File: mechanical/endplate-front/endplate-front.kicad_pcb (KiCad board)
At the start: 2 copper layers, 88 x 38 mm, 0 parts

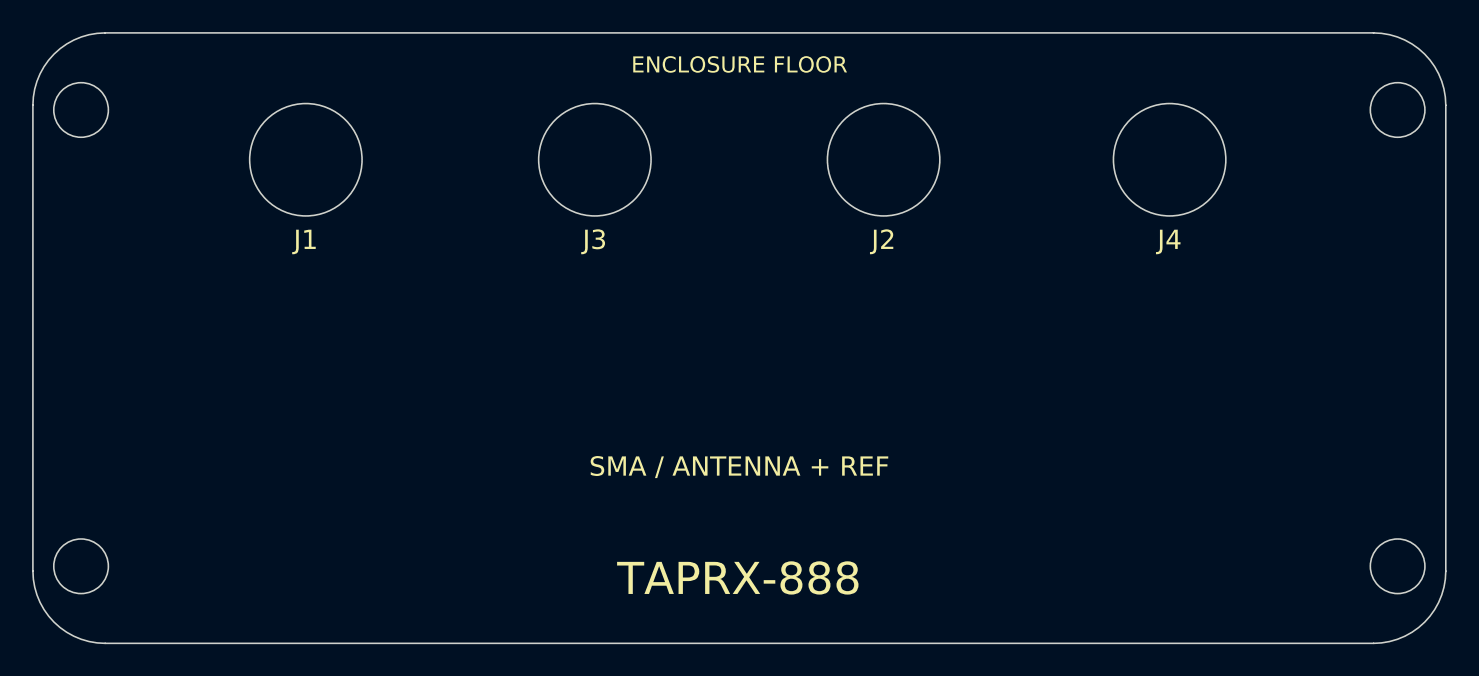
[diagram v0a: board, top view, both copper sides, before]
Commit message: mechanical: label front-plate SMA cutouts by function
Silkscreen the four SMA pass-throughs with their functions instead of bare
designators: J1 RF IN, J3 SPARE, J2 TIMESYNC IN, J4 EXT REF (function name +
small Jx under each hole).

Co-Authored-By: Claude Opus 4.8 <noreply@anthropic.com>
Claude-Session: https://claude.ai/code/session_019A4jkTeNPLki8CdfTWEUwM
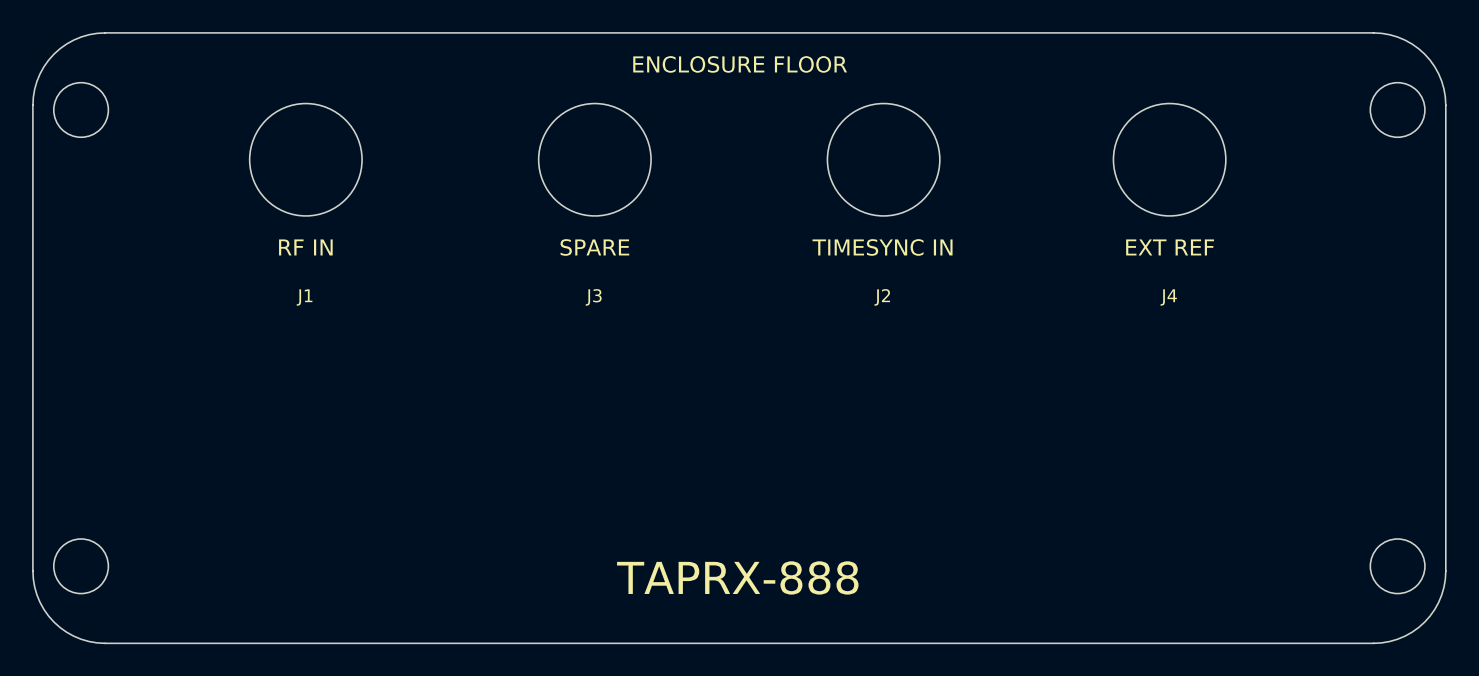
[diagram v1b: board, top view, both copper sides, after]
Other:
- board text added: "EXT REF"
- board text added: "RF IN"
- board text added: "SPARE"
- board text added: "TIMESYNC IN"
- board text removed: "SMA / ANTENNA + REF"
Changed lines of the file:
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@@
 		(layer "Edge.Cuts")
 	)
-	(gr_text "J1"
-		(at 17.0 12.9)
+	(gr_text "RF IN"
+		(at 17.0 13.4)
 		(layer "F.SilkS")
 		(effects
 			(font
-				(size 1.2 1.2)
-				(thickness 0.2)
+				(size 1.0 1.0)
+				(thickness 0.15)
+			)
+		)
+	)
+	(gr_text "J1"
+		(at 17.0 16.4)
+		(layer "F.SilkS")
+		(effects
+			(font
+				(size 0.8 0.8)
+				(thickness 0.12)
 			)
 		)
@@
 		(layer "Edge.Cuts")
 	)
-	(gr_text "J3"
-		(at 35.0 12.9)
+	(gr_text "SPARE"
+		(at 35.0 13.4)
 		(layer "F.SilkS")
 		(effects
 			(font
-				(size 1.2 1.2)
-				(thickness 0.2)
+				(size 1.0 1.0)
+				(thickness 0.15)
+			)
+		)
+	)
+	(gr_text "J3"
+		(at 35.0 16.4)
+		(layer "F.SilkS")
+		(effects
+			(font
+				(size 0.8 0.8)
+				(thickness 0.12)
 			)
 		)
@@
 		(layer "Edge.Cuts")
 	)
-	(gr_text "J2"
-		(at 52.986 12.9)
+	(gr_text "TIMESYNC IN"
+		(at 52.986 13.4)
 		(layer "F.SilkS")
 		(effects
 			(font
-				(size 1.2 1.2)
-				(thickness 0.2)
+				(size 1.0 1.0)
+				(thickness 0.15)
+			)
+		)
+	)
+	(gr_text "J2"
+		(at 52.986 16.4)
+		(layer "F.SilkS")
+		(effects
+			(font
+				(size 0.8 0.8)
+				(thickness 0.12)
 			)
 		)
@@
 		(layer "Edge.Cuts")
 	)
-	(gr_text "J4"
-		(at 70.8 12.9)
+	(gr_text "EXT REF"
+		(at 70.8 13.4)
 		(layer "F.SilkS")
 		(effects
 			(font
-				(size 1.2 1.2)
-				(thickness 0.2)
+				(size 1.0 1.0)
+				(thickness 0.15)
+			)
+		)
+	)
+	(gr_text "J4"
+		(at 70.8 16.4)
+		(layer "F.SilkS")
+		(effects
+			(font
+				(size 0.8 0.8)
+				(thickness 0.12)
 			)
 		)
@@
 			)
 		)
-	)
-	(gr_text "SMA / ANTENNA + REF"
-		(at 44.0 27.02)
-		(layer "F.SilkS")
-		(effects
-			(font
-				(size 1.2 1.2)
-				(thickness 0.2)
-			)
-		)

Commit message: mechanical: move connector labels to the floor side (exposed panel)
The interior side of each cutout is hidden behind the board once assembled, so
put the silkscreen on the floor side (toward the top edge): SMA function names
above their holes, USB label above its opening. Drop the per-hole J# from silk
(space is tight on the exposed strip) and record the J#->function map + floor
orientation in the Cmts.User note instead.

Co-Authored-By: Claude Opus 4.8 <noreply@anthropic.com>
Claude-Session: https://claude.ai/code/session_019A4jkTeNPLki8CdfTWEUwM
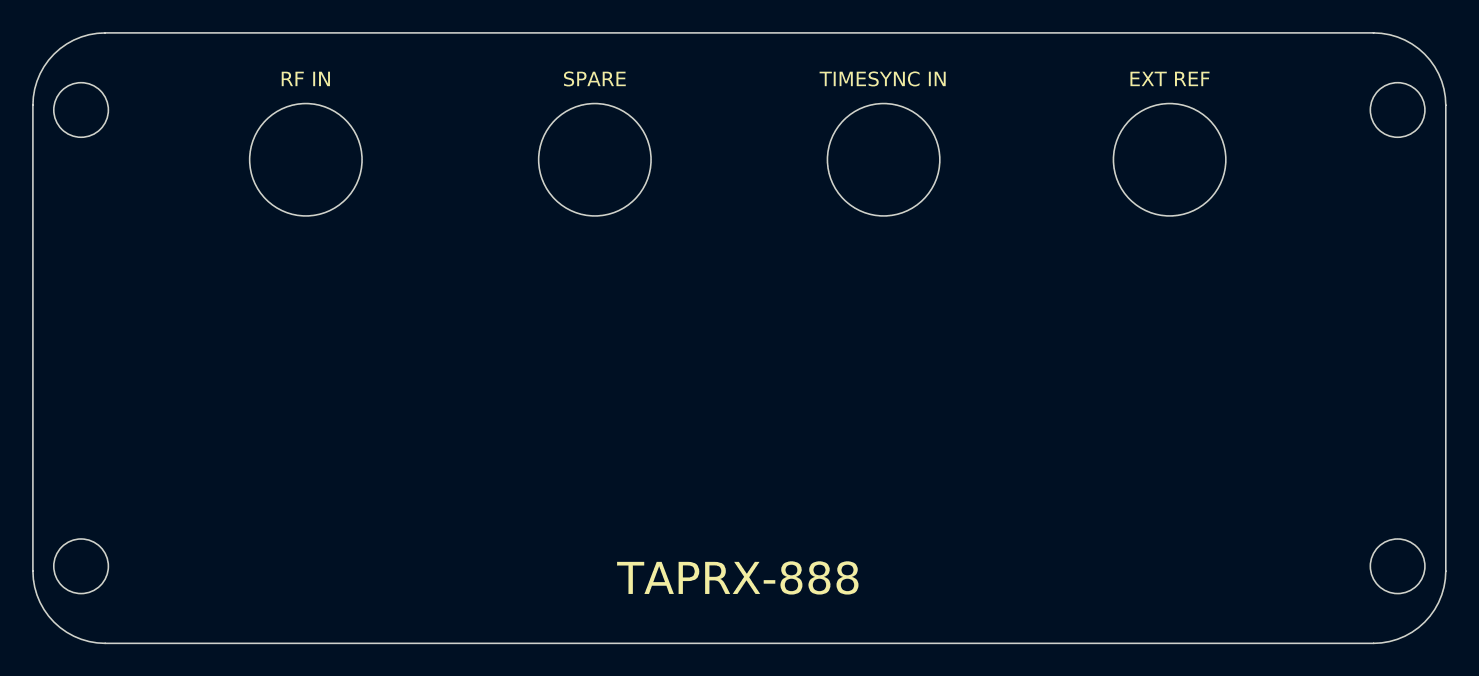
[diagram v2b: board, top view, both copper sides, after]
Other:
- board text added: "Outline+M3 corner holes from enclosure DXF (88x38 R4.5, holes Ø3.4 @ +/-41,+/-14.21). Connector Y set from measured 7.9mm PCB rail height above enclosure floor (TOP edge, Y=0). SMA holes Ø7.0 at plate Y 7.90 (edge-launch, board plane). USB opening 12.5x12.7 at plate Y 14.79 (bottom flush to board top surface; connector rises 12.2 into box). Floor = connector edge (top, Y=0). SMA: J1=RF IN J3=SPAR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"
- board text removed: "ENCLOSURE FLOOR"
- board text removed: "J1"
- board text removed: "J2"
- board text removed: "J3"
- board text removed: "J4"
- board text removed: "Outline+M3 corner holes from enclosure DXF (88x38 R4.5, holes Ø3.4 @ +/-41,+/-14.21). Connector Y set from measured 7.9mm PCB rail height above enclosure floor (TOP edge, Y=0). SMA holes Ø7.0 at plate Y 7.90 (edge-launch, board plane). USB opening 12.5x12.7 at plate Y 14.79 (bottom flush to board top surface; connector rises 12.2 into box). Open in KiCad 10 to confirm parse."
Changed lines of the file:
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@@
 	)
 	(gr_text "RF IN"
-		(at 17.0 13.4)
+		(at 17.0 2.9)
 		(layer "F.SilkS")
 		(effects
 			(font
-				(size 1.0 1.0)
+				(size 0.9 0.9)
 				(thickness 0.15)
-			)
-		)
-	)
-	(gr_text "J1"
-		(at 17.0 16.4)
-		(layer "F.SilkS")
-		(effects
-			(font
-				(size 0.8 0.8)
-				(thickness 0.12)
 			)
 		)
@@
 	)
 	(gr_text "SPARE"
-		(at 35.0 13.4)
+		(at 35.0 2.9)
 		(layer "F.SilkS")
 		(effects
 			(font
-				(size 1.0 1.0)
+				(size 0.9 0.9)
 				(thickness 0.15)
-			)
-		)
-	)
-	(gr_text "J3"
-		(at 35.0 16.4)
-		(layer "F.SilkS")
-		(effects
-			(font
-				(size 0.8 0.8)
-				(thickness 0.12)
 			)
 		)
@@
 	)
 	(gr_text "TIMESYNC IN"
-		(at 52.986 13.4)
+		(at 52.986 2.9)
 		(layer "F.SilkS")
 		(effects
 			(font
-				(size 1.0 1.0)
+				(size 0.9 0.9)
 				(thickness 0.15)
-			)
-		)
-	)
-	(gr_text "J2"
-		(at 52.986 16.4)
-		(layer "F.SilkS")
-		(effects
-			(font
-				(size 0.8 0.8)
-				(thickness 0.12)
 			)
 		)
@@
 	)
 	(gr_text "EXT REF"
-		(at 70.8 13.4)
+		(at 70.8 2.9)
 		(layer "F.SilkS")
 		(effects
 			(font
-				(size 1.0 1.0)
-				(thickness 0.15)
-			)
-		)
-	)
-	(gr_text "J4"
-		(at 70.8 16.4)
-		(layer "F.SilkS")
-		(effects
-			(font
-				(size 0.8 0.8)
-				(thickness 0.12)
-			)
-		)
-	)
-	(gr_text "ENCLOSURE FLOOR"
-		(at 44.0 2)
-		(layer "F.SilkS")
-		(effects
-			(font
-				(size 1.0 1.0)
+				(size 0.9 0.9)
 				(thickness 0.15)
 			)
@@
 		)
 	)
-	(gr_text "Outline+M3 corner holes from enclosure DXF (88x38 R4.5, holes Ø3.4 @ +/-41,+/-14.21). Connector Y set from measured 7.9mm PCB rail height above enclosure floor (TOP edge, Y=0). SMA holes Ø7.0 at plate Y 7.90 (edge-launch, board plane). USB opening 12.5x12.7 at plate Y 14.79 (bottom flush to board top surface; connector rises 12.2 into box). Open in KiCad 10 to confirm parse."
+	(gr_text "Outline+M3 corner holes from enclosure DXF (88x38 R4.5, holes Ø3.4 @ +/-41,+/-14.21). Connector Y set from measured 7.9mm PCB rail height above enclosure floor (TOP edge, Y=0). SMA holes Ø7.0 at plate Y 7.90 (edge-launch, board plane). USB opening 12.5x12.7 at plate Y 14.79 (bottom flush to board top surface; connector rises 12.2 into box). Floor = connector edge (top, Y=0). SMA: J1=RF IN J3=SPARE J2=TIMESYNC IN J4=EXT REF. Open in KiCad 10 to confirm parse."
 		(at 44.0 42.02)
 		(layer "Cmts.User")

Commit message: mechanical: logos to front mid-band, big TAPRX-888 title on rear
Per review: put the three logos (TAPR/TIS/HamSCI) on the FRONT, scaled 1.2 across
the open mid-band that was empty (X8-80, Y14-26), keeping the SMA cutouts, labels
and wordmark. The REAR drops the logos entirely and uses the open area below the
USB opening for a large two-line silk title: 'TAPRX-888' (size 3.5) over
'HF SDR Receiver' (size 1.6), same F.SilkS stroke font as the connector labels.

Co-Authored-By: Claude Opus 4.8 <noreply@anthropic.com>
Claude-Session: https://claude.ai/code/session_019A4jkTeNPLki8CdfTWEUwM
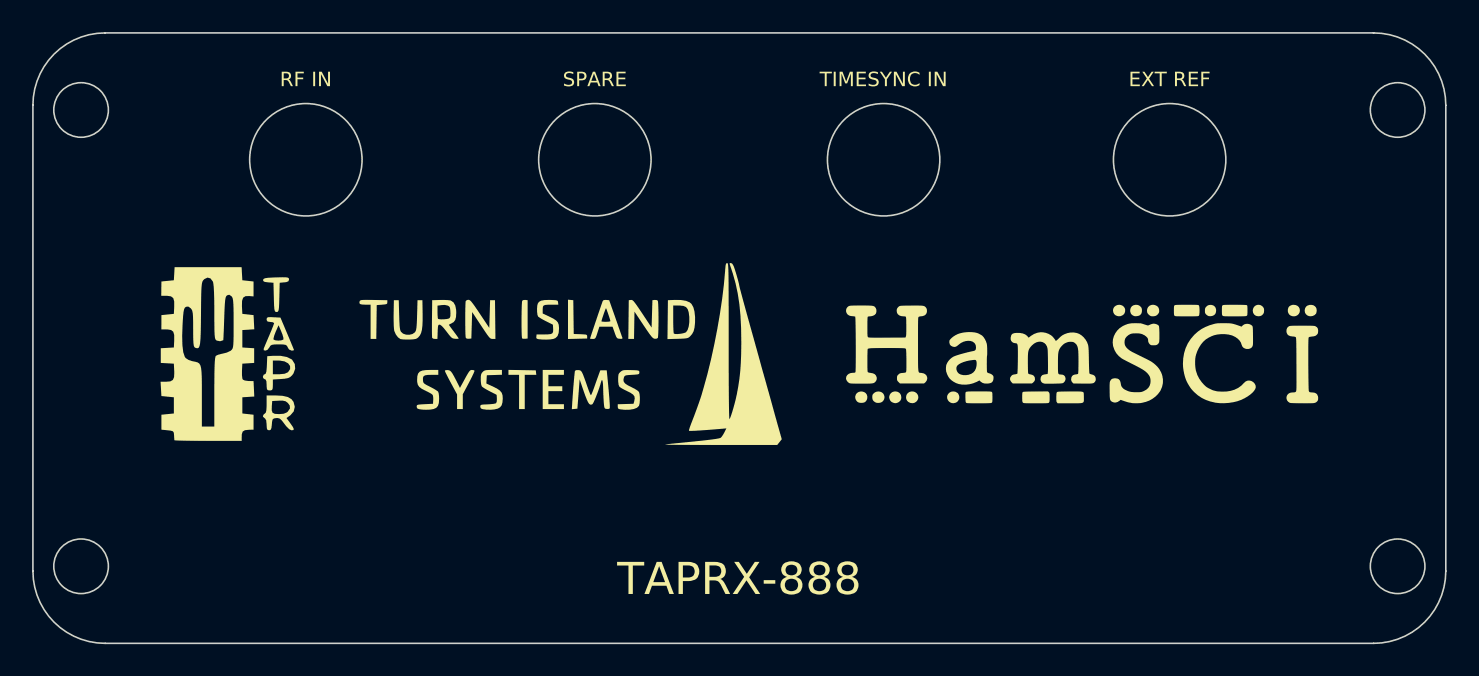
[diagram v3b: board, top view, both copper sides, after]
